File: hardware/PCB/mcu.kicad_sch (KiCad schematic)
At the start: 39 parts, among them J2 Conn_02x05_Odd_Even, SW1 RESET, SW2 PROG

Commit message: Update mcu.kicad_sch
usb connector
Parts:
- removed C28, C29: C, symbol Device:C
- added J3: USB_C_Receptacle_USB2.0_16P, symbol Connector:USB_C_Receptacle_USB2.0_16P
- added R17: 5.1k, symbol Device:R_US
- added U4: 32 MHz, CustomFootprints:ECS-3225, symbol CustomSymbols:ECS-3225MVLC
- added Y1: Crystal, symbol Device:Crystal
- C30, C31: value C -> 15p
- R16: value R -> 5.1k
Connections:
- net +3.3V: now also U4.4 (VDD)
- net GND: now also R16.2, J3.A1 (GND), J3.A12 (GND), J3.B1 (GND), J3.B12 (GND), J3.S1 (SHIELD), R17.1, U4.2 (GND)
- net OSC32_IN: now also Y1.1
- net OSC32_OUT: now also Y1.2
- net OSC_IN: now also U4.3 (OUT)
- net USB_DM: now also J3.A7 (D-), J3.B7 (D-)
- net USB_DP: now also J3.A6 (D+), J3.B6 (D+)
- net at R16.1: now also J3.A5 (CC1)
- net OSC_OUT: no longer names the net of U?.32 (PH1)
- net OSC_OUT: no longer R16.2
- net USB_VBUS renamed VBUS
- net VBUS: now also J3.A4 (VBUS), J3.A9 (VBUS), J3.B4 (VBUS), J3.B9 (VBUS)
- new net: J3.B5 (CC2), R17.2
- no-connect marks 9 -> 13
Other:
- note added: "HSE & LSE"
- note added: "USB"
- moved on the sheet: C27, C30, C31, C5, C51, C6, J2, R14, R15, SW1, SW2, U?

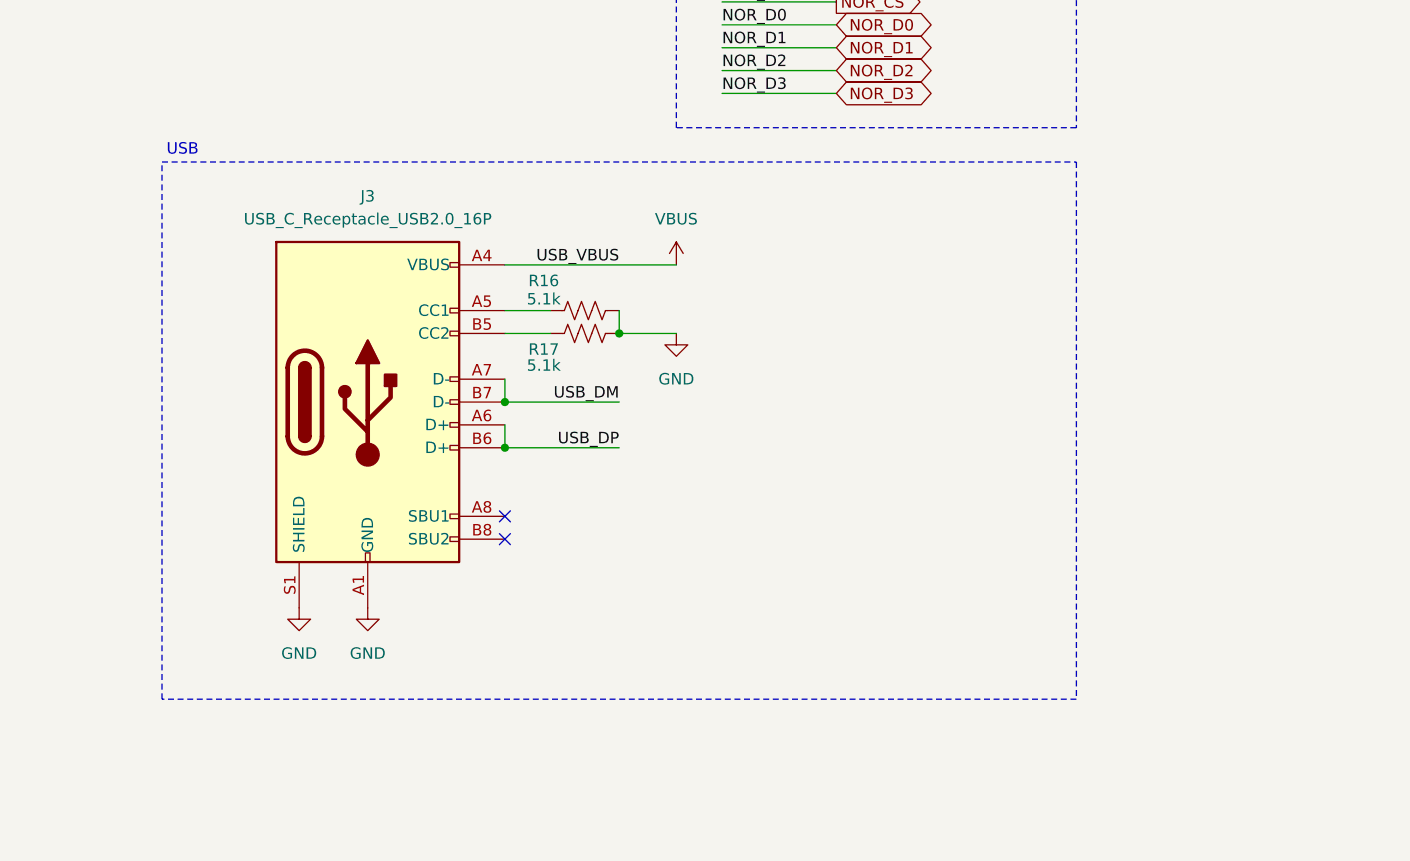
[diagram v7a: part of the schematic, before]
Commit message: Update mcu.kicad_sch
usb shield
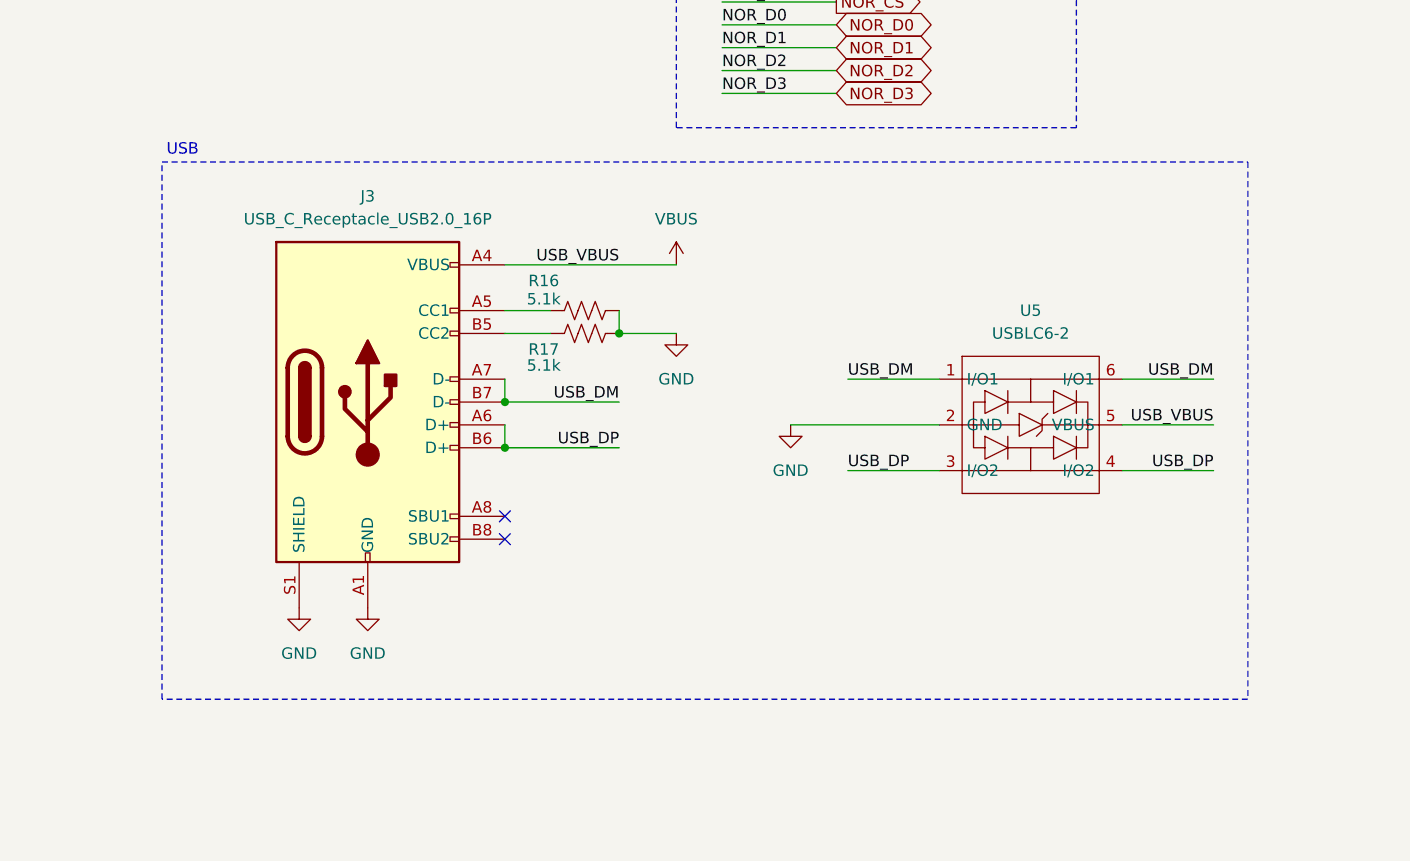
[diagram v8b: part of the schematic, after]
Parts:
- added U5: USBLC6-2, Package_TO_SOT_SMD:SOT-23-6, symbol CustomSymbols:USBLC6-2
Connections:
- net GND: now also U5.2 (GND)
- net USB_DM: now also U5.1 (I/O1), U5.6 (I/O1)
- net USB_DP: now also U5.3 (I/O2), U5.4 (I/O2)
- net VBUS: now also U5.5 (VBUS)
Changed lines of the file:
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@@
 	(rectangle
 		(start 292.1 168.91)
-		(end 393.7 228.6)
+		(end 412.75 228.6)
 		(stroke
 			(width 0)
@@
 	(wire
 		(pts
+			(xy 378.46 198.12) (xy 361.95 198.12)
+		)
+		(stroke
+			(width 0)
+			(type default)
+		)
+	)
+	(wire
+		(pts
 			(xy 45.72 162.56) (xy 50.8 162.56)
 		)
@@
 	(wire
 		(pts
+			(xy 378.46 203.2) (xy 368.3 203.2)
+		)
+		(stroke
+			(width 0)
+			(type default)
+		)
+	)
+	(wire
+		(pts
 			(xy 256.54 166.37) (xy 269.24 166.37)
 		)
@@
 	(wire
 		(pts
+			(xy 398.78 193.04) (xy 408.94 193.04)
+		)
+		(stroke
+			(width 0)
+			(type default)
+		)
+	)
+	(wire
+		(pts
 			(xy 147.32 186.69) (xy 160.02 186.69)
 		)
@@
 	(wire
 		(pts
+			(xy 398.78 203.2) (xy 408.94 203.2)
+		)
+		(stroke
+			(width 0)
+			(type default)
+		)
+	)
+	(wire
+		(pts
 			(xy 87.63 76.2) (xy 93.98 76.2)
 		)
@@
 	(wire
 		(pts
+			(xy 378.46 193.04) (xy 368.3 193.04)
+		)
+		(stroke
+			(width 0)
+			(type default)
+		)
+	)
+	(wire
+		(pts
 			(xy 147.32 212.09) (xy 160.02 212.09)
 		)
@@
 	(wire
 		(pts
+			(xy 398.78 198.12) (xy 408.94 198.12)
+		)
+		(stroke
+			(width 0)
+			(type default)
+		)
+	)
+	(wire
+		(pts
 			(xy 148.59 54.61) (xy 160.02 54.61)
 		)
@@
 		)
 	)
+	(label "USB_DP"
+		(at 368.3 203.2 0)
+		(effects
+			(font
+				(size 1.27 1.27)
+			)
+			(justify left bottom)
+		)
+	)
 	(label "VSS"
 		(at 205.74 255.27 90)
@@
 		)
 	)
+	(label "USB_DP"
+		(at 408.94 203.2 180)
+		(effects
+			(font
+				(size 1.27 1.27)
+			)
+			(justify right bottom)
+		)
+	)
 	(label "LCD_HSYNC"
 		(at 354.33 91.44 0)
@@
 		)
 	)
+	(label "USB_VBUS"
+		(at 408.94 198.12 180)
+		(effects
+			(font
+				(size 1.27 1.27)
+			)
+			(justify right bottom)
+		)
+	)
 	(label "LCD_G2"
 		(at 354.33 48.26 0)
@@
 		)
 	)
+	(label "USB_DM"
+		(at 368.3 193.04 0)
+		(effects
+			(font
+				(size 1.27 1.27)
+			)
+			(justify left bottom)
+		)
+	)
 	(label "LCD_R7"
 		(at 354.33 40.64 0)
@@
 		)
 	)
+	(label "USB_DM"
+		(at 408.94 193.04 180)
+		(effects
+			(font
+				(size 1.27 1.27)
+			)
+			(justify right bottom)
+		)
+	)
 	(label "LCD_R3"
 		(at 269.24 92.71 180)
@@
 	)
 	(symbol
+		(lib_id "CustomSymbols:USBLC6-2")
+		(at 388.62 198.12 0)
+		(unit 1)
+		(exclude_from_sim no)
+		(in_bom yes)
+		(on_board yes)
+		(dnp no)
+		(fields_autoplaced yes)
+		(property "Reference" "U5"
+			(at 388.62 185.42 0)
+			(effects
+				(font
+					(size 1.27 1.27)
+				)
+			)
+		)
+		(property "Value" "USBLC6-2"
+			(at 388.62 187.96 0)
+			(effects
+				(font
+					(size 1.27 1.27)
+				)
+			)
+		)
+		(property "Footprint" "Package_TO_SOT_SMD:SOT-23-6"
+			(at 388.874 207.772 0)
+			(effects
+				(font
+					(size 1.27 1.27)
+				)
+				(hide yes)
+			)
+		)
+		(property "Datasheet" "file:///C:/Users/griff/Downloads/usblc6-2.pdf"
+			(at 388.112 211.836 0)
+			(effects
+				(font
+					(size 1.27 1.27)
+				)
+				(hide yes)
+			)
+		)
+		(property "Description" "Very low capacitance ESD protection for USB 2.0"
+			(at 388.112 209.804 0)
+			(effects
+				(font
+					(size 1.27 1.27)
+				)
+				(hide yes)
+			)
+		)
+		(pin "2"
+		)
+		(pin "3"
+		)
+		(pin "5"
+		)
+		(pin "1"
+		)
+		(pin "6"
+		)
+		(pin "4"
+		)
+		(instances
+			(project ""
+				(path "/2826ff7c-9767-4078-8ea2-1cd3a432abf3/85803a25-8176-4fac-b186-52d9676cab71"
+					(reference "U5")
+					(unit 1)
+				)
+			)
+		)
+	)
+	(symbol
 		(lib_id "Device:R_US")
 		(at 339.09 187.96 270)
@@
 					(unit 1)
 				)
+			)
+		)
+	)
+	(symbol
+		(lib_id "power:GND")
+		(at 361.95 198.12 0)
+		(unit 1)
+		(exclude_from_sim no)
+		(in_bom yes)
+		(on_board yes)
+		(dnp no)
+		(property "Reference" "#PWR052"
+			(at 361.95 204.47 0)
+			(effects
+				(font
+					(size 1.27 1.27)
+				)
+				(hide yes)
+			)
+		)
+		(property "Value" "GND"
+			(at 361.95 203.2 0)
+			(effects
+				(font
+					(size 1.27 1.27)
+				)
+			)
+		)
+		(property "Footprint" ""
+			(at 361.95 198.12 0)
+			(effects
+				(font
+					(size 1.27 1.27)
+				)
+				(hide yes)
+			)
+		)
+		(property "Datasheet" ""
+			(at 361.95 198.12 0)
+			(effects
+				(font
+					(size 1.27 1.27)
+				)
+				(hide yes)
+			)
+		)
+		(property "Description" "Power symbol creates a global label with name \"GND\" , ground"
+			(at 361.95 198.12 0)
+			(effects
+				(font
+					(size 1.27 1.27)
+				)
+				(hide yes)
+			)
+		)
+		(pin "1"
+		)
+		(instances
+			(project "TopiaryTrimbot"
+				(path "/2826ff7c-9767-4078-8ea2-1cd3a432abf3/85803a25-8176-4fac-b186-52d9676cab71"
+					(reference "#PWR052")
+					(unit 1)
+				)
